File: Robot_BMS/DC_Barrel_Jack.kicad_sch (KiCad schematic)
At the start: 15 parts, among them J2 DCJ200-10-A-XX-K_REVA, U7 TPS56637RPAR

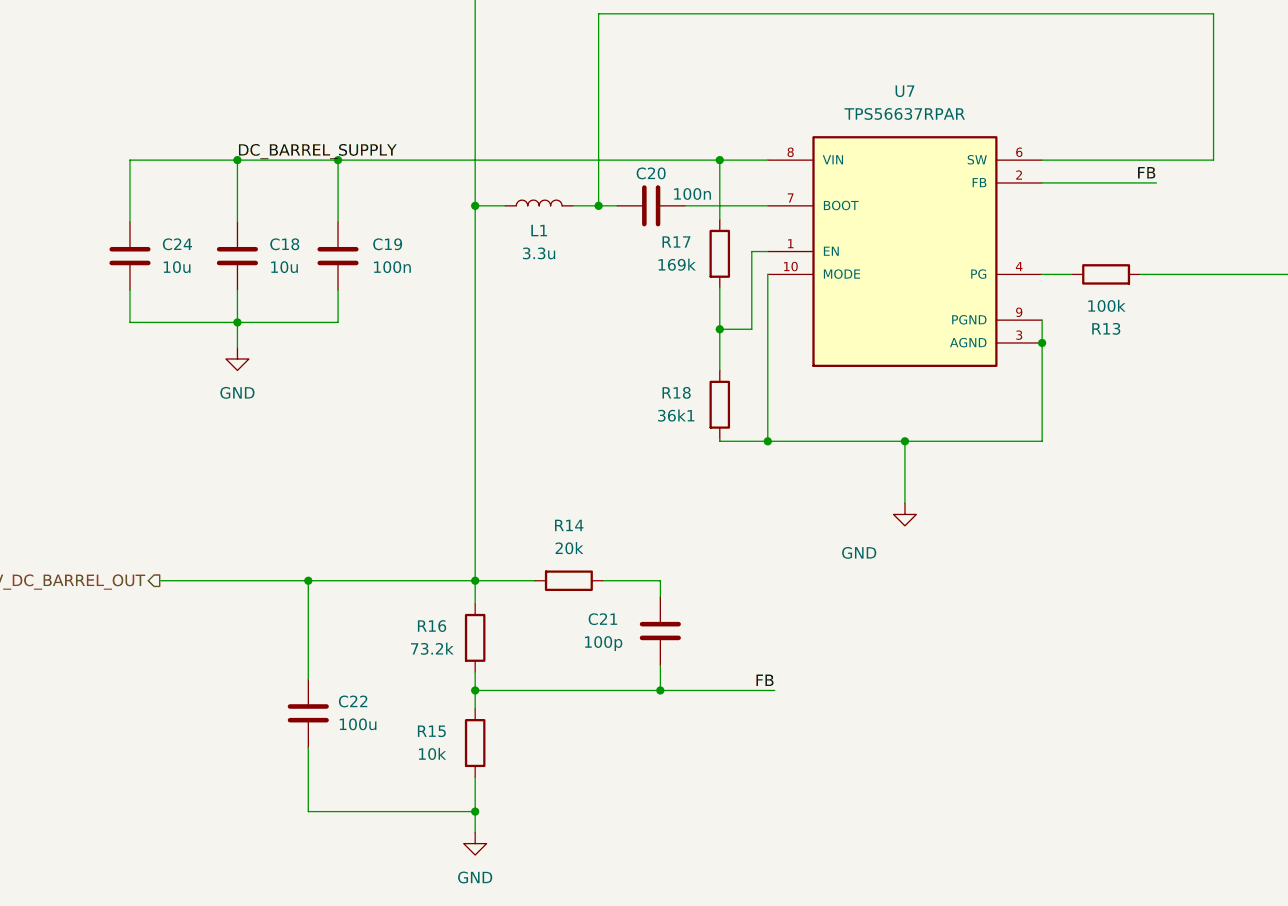
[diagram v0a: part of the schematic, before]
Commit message: implementing sepic converter for Solar power input
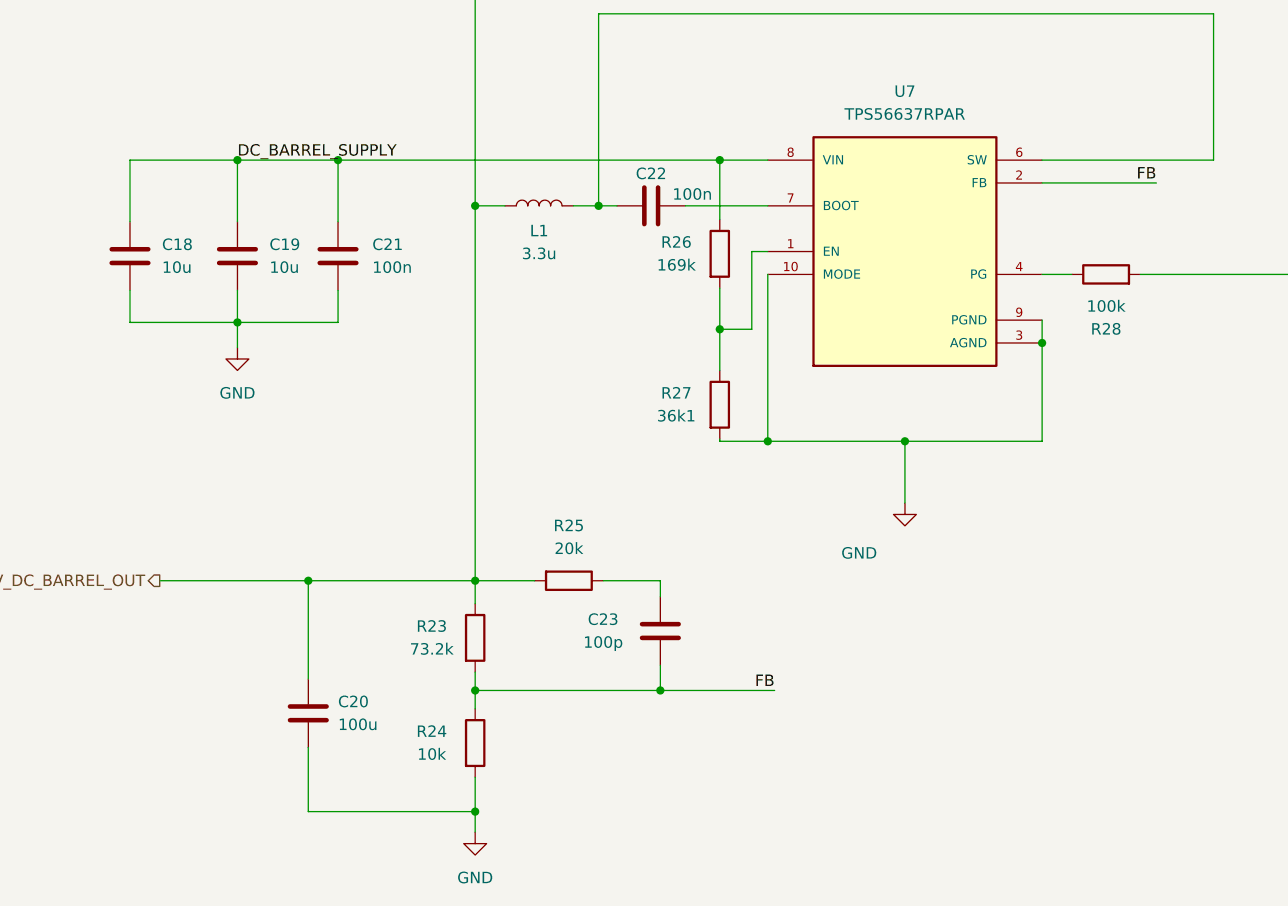
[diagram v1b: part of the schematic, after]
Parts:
- renumbered C24 to C18, C18 to C19, C22 to C20, C19 to C21, C20 to C22, C21 to C23, R16 to R23, R15 to R24, R14 to R25, R17 to R26, R18 to R27, R13 to R28
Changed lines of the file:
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@@
 		(on_board yes)
 		(dnp no)
-		(property "Reference" "R13"
+		(property "Reference" "R28"
 			(at 156.464 92.456 90)
 			(effects
@@
 			(project ""
 				(path "/72551b1c-3d40-4199-8911-e5b015f4abec/7a60a594-7330-4ecb-a3c9-8c0f96aa21b4"
-					(reference "R13")
+					(reference "R28")
 					(unit 1)
 				)
@@
 		(dnp no)
 		(fields_autoplaced yes)
-		(property "Reference" "C18"
+		(property "Reference" "C19"
 			(at 63.5 83.0579 0)
 			(effects
@@
 			(project ""
 				(path "/72551b1c-3d40-4199-8911-e5b015f4abec/7a60a594-7330-4ecb-a3c9-8c0f96aa21b4"
-					(reference "C18")
+					(reference "C19")
 					(unit 1)
 				)
@@
 		(on_board yes)
 		(dnp no)
-		(property "Reference" "#PWR021"
+		(property "Reference" "#PWR022"
 			(at 134.112 118.11 0)
 			(effects
@@
 			(project "Robot_BMS"
 				(path "/72551b1c-3d40-4199-8911-e5b015f4abec/7a60a594-7330-4ecb-a3c9-8c0f96aa21b4"
-					(reference "#PWR021")
+					(reference "#PWR022")
 					(unit 1)
 				)
@@
 		(dnp no)
 		(fields_autoplaced yes)
-		(property "Reference" "#PWR022"
+		(property "Reference" "#PWR020"
 			(at 59.944 100.838 0)
 			(effects
@@
 			(project "Robot_BMS"
 				(path "/72551b1c-3d40-4199-8911-e5b015f4abec/7a60a594-7330-4ecb-a3c9-8c0f96aa21b4"
-					(reference "#PWR022")
+					(reference "#PWR020")
 					(unit 1)
 				)
@@
 		(dnp no)
 		(fields_autoplaced yes)
-		(property "Reference" "#PWR023"
+		(property "Reference" "#PWR021"
 			(at 86.36 154.686 0)
 			(effects
@@
 			(project "Robot_BMS"
 				(path "/72551b1c-3d40-4199-8911-e5b015f4abec/7a60a594-7330-4ecb-a3c9-8c0f96aa21b4"
-					(reference "#PWR023")
+					(reference "#PWR021")
 					(unit 1)
 				)
@@
 		(on_board yes)
 		(dnp no)
-		(property "Reference" "C21"
+		(property "Reference" "C23"
 			(at 100.584 124.714 0)
 			(effects
@@
 			(project "Robot_BMS"
 				(path "/72551b1c-3d40-4199-8911-e5b015f4abec/7a60a594-7330-4ecb-a3c9-8c0f96aa21b4"
-					(reference "C21")
+					(reference "C23")
 					(unit 1)
 				)
@@
 		(dnp no)
 		(fields_autoplaced yes)
-		(property "Reference" "C22"
+		(property "Reference" "C20"
 			(at 71.12 133.8579 0)
 			(effects
@@
 			(project "Robot_BMS"
 				(path "/72551b1c-3d40-4199-8911-e5b015f4abec/7a60a594-7330-4ecb-a3c9-8c0f96aa21b4"
-					(reference "C22")
+					(reference "C20")
 					(unit 1)
 				)
@@
 		(on_board yes)
 		(dnp no)
-		(property "Reference" "R18"
+		(property "Reference" "R27"
 			(at 108.712 99.568 0)
 			(effects
@@
 			(project "Robot_BMS"
 				(path "/72551b1c-3d40-4199-8911-e5b015f4abec/7a60a594-7330-4ecb-a3c9-8c0f96aa21b4"
-					(reference "R18")
+					(reference "R27")
 					(unit 1)
 				)
@@
 		(on_board yes)
 		(dnp no)
-		(property "Reference" "R15"
+		(property "Reference" "R24"
 			(at 81.534 137.16 0)
 			(effects
@@
 			(project "Robot_BMS"
 				(path "/72551b1c-3d40-4199-8911-e5b015f4abec/7a60a594-7330-4ecb-a3c9-8c0f96aa21b4"
-					(reference "R15")
+					(reference "R24")
 					(unit 1)
 				)
@@
 		(dnp no)
 		(fields_autoplaced yes)
-		(property "Reference" "C19"
+		(property "Reference" "C21"
 			(at 74.93 83.0579 0)
 			(effects
@@
 			(project "Robot_BMS"
 				(path "/72551b1c-3d40-4199-8911-e5b015f4abec/7a60a594-7330-4ecb-a3c9-8c0f96aa21b4"
-					(reference "C19")
+					(reference "C21")
 					(unit 1)
 				)
@@
 		(on_board yes)
 		(dnp no)
-		(property "Reference" "R17"
+		(property "Reference" "R26"
 			(at 108.712 82.804 0)
 			(effects
@@
 			(project "Robot_BMS"
 				(path "/72551b1c-3d40-4199-8911-e5b015f4abec/7a60a594-7330-4ecb-a3c9-8c0f96aa21b4"
-					(reference "R17")
+					(reference "R26")
 					(unit 1)
 				)
@@
 		(dnp no)
 		(fields_autoplaced yes)
-		(property "Reference" "C24"
+		(property "Reference" "C18"
 			(at 51.562 83.0579 0)
 			(effects
@@
 			(project "Robot_BMS"
 				(path "/72551b1c-3d40-4199-8911-e5b015f4abec/7a60a594-7330-4ecb-a3c9-8c0f96aa21b4"
-					(reference "C24")
+					(reference "C18")
 					(unit 1)
 				)
@@
 		(dnp no)
 		(fields_autoplaced yes)
-		(property "Reference" "#PWR020"
+		(property "Reference" "#PWR023"
 			(at 212.852 85.09 0)
 			(effects
@@
 			(project ""
 				(path "/72551b1c-3d40-4199-8911-e5b015f4abec/7a60a594-7330-4ecb-a3c9-8c0f96aa21b4"
-					(reference "#PWR020")
+					(reference "#PWR023")
 					(unit 1)
 				)
@@
 		(on_board yes)
 		(dnp no)
-		(property "Reference" "R16"
+		(property "Reference" "R23"
 			(at 81.534 125.476 0)
 			(effects
@@
 			(project "Robot_BMS"
 				(path "/72551b1c-3d40-4199-8911-e5b015f4abec/7a60a594-7330-4ecb-a3c9-8c0f96aa21b4"
-					(reference "R16")
+					(reference "R23")
 					(unit 1)
 				)
@@
 		(on_board yes)
 		(dnp no)
-		(property "Reference" "C20"
+		(property "Reference" "C22"
 			(at 105.918 75.184 90)
 			(effects
@@
 			(project "Robot_BMS"
 				(path "/72551b1c-3d40-4199-8911-e5b015f4abec/7a60a594-7330-4ecb-a3c9-8c0f96aa21b4"
-					(reference "C20")
+					(reference "C22")
 					(unit 1)
 				)
@@
 		(on_board yes)
 		(dnp no)
-		(property "Reference" "R14"
+		(property "Reference" "R25"
 			(at 96.774 114.3 90)
 			(effects
@@
 			(project "Robot_BMS"
 				(path "/72551b1c-3d40-4199-8911-e5b015f4abec/7a60a594-7330-4ecb-a3c9-8c0f96aa21b4"
-					(reference "R14")
-					(unit 1)
-				)
+					(reference "R25")
+					(unit 1)
+				)

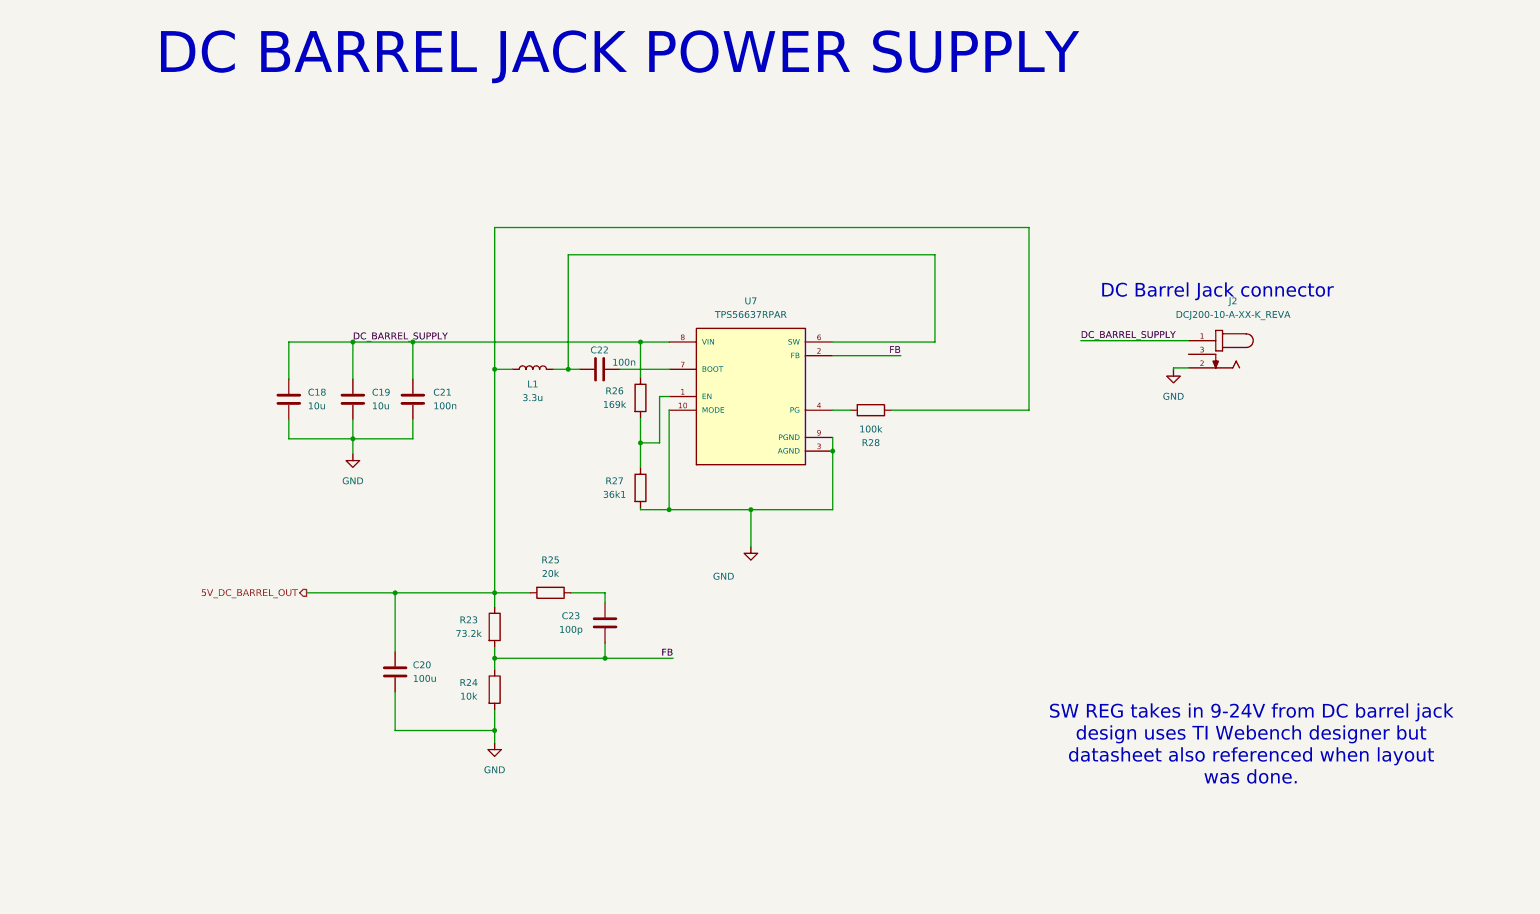
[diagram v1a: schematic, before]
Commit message: solar charger set to 15V
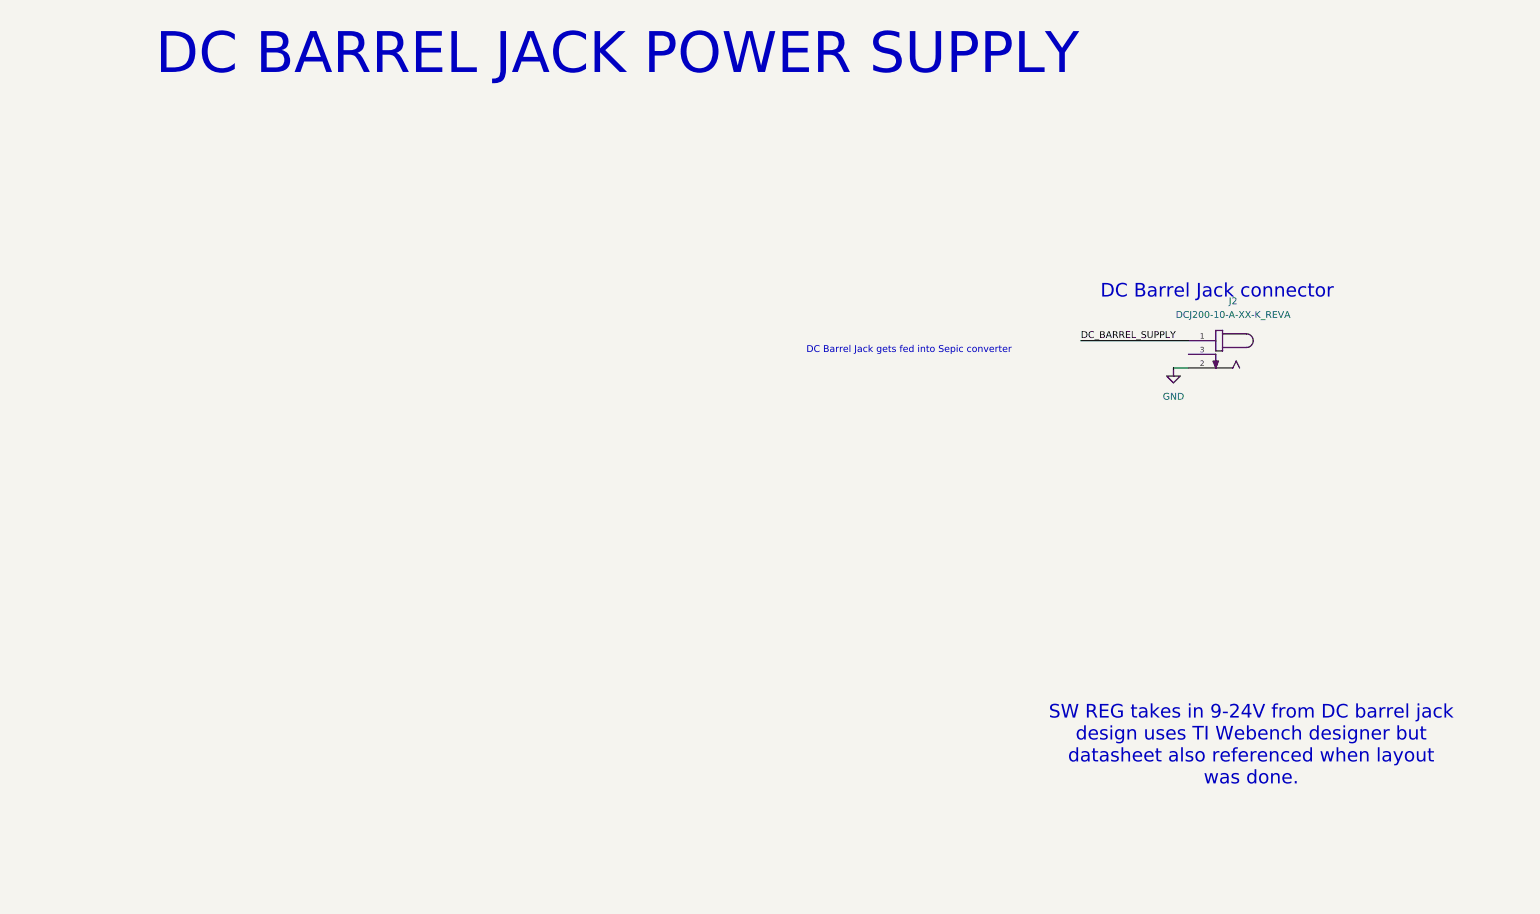
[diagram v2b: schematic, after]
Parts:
- removed C18, C19: 10u, symbol Device:C
- removed C20: 100u, symbol Device:C
- removed C21, C22: 100n, symbol Device:C
- removed C23: 100p, symbol Device:C
- removed L1: 3.3u, symbol Device:L
- removed R23: 73.2k, symbol Device:R
- removed R24: 10k, symbol Device:R
- removed R25: 20k, symbol Device:R
- removed R26: 169k, symbol Device:R
- removed R27: 36k1, symbol Device:R
- removed R28: 100k, symbol Device:R
- removed U7: TPS56637RPAR, TPS56637RPAR:CONV_TPS56637RPAR, symbol TPS56637RPAR:TPS56637RPAR
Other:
- note added: "DC Barrel Jack gets fed into Sepic converter"
